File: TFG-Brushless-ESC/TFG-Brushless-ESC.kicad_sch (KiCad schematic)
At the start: 41 parts, among them J1 POWER IN, J2 USB C Receptacle, J3 SWD, J4 MOTOR, SW1 BOOT0, SW2 NRST, SW3 USER, U1 LM317, U2 STM32F411CEUx, Y1 25MHz, Y2 32.768kHz

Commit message: Renaming
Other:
- company: (none) -> Adrián Teixeira de Uña
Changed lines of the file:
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@@
 	(title_block
 		(title "RTSpeed")
+		(date "2024-04-17")
+		(rev "alpha-1.0")
+		(company "Adrián Teixeira de Uña")
 	)
 	(junction

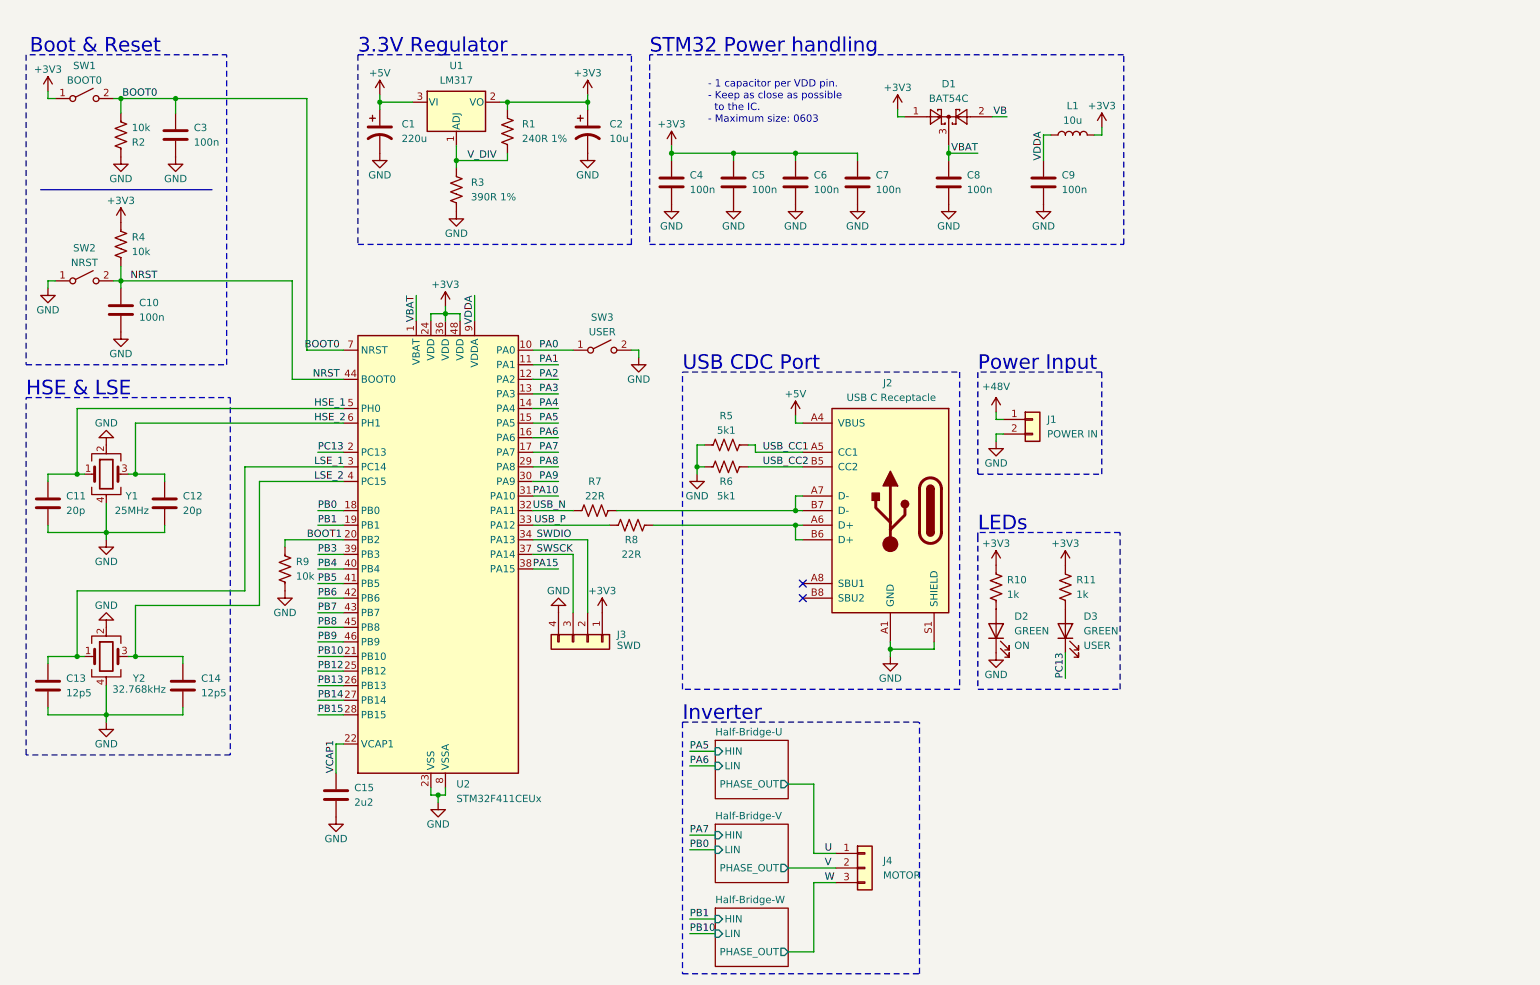
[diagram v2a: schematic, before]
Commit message: Attempt at implementing regenerative braking
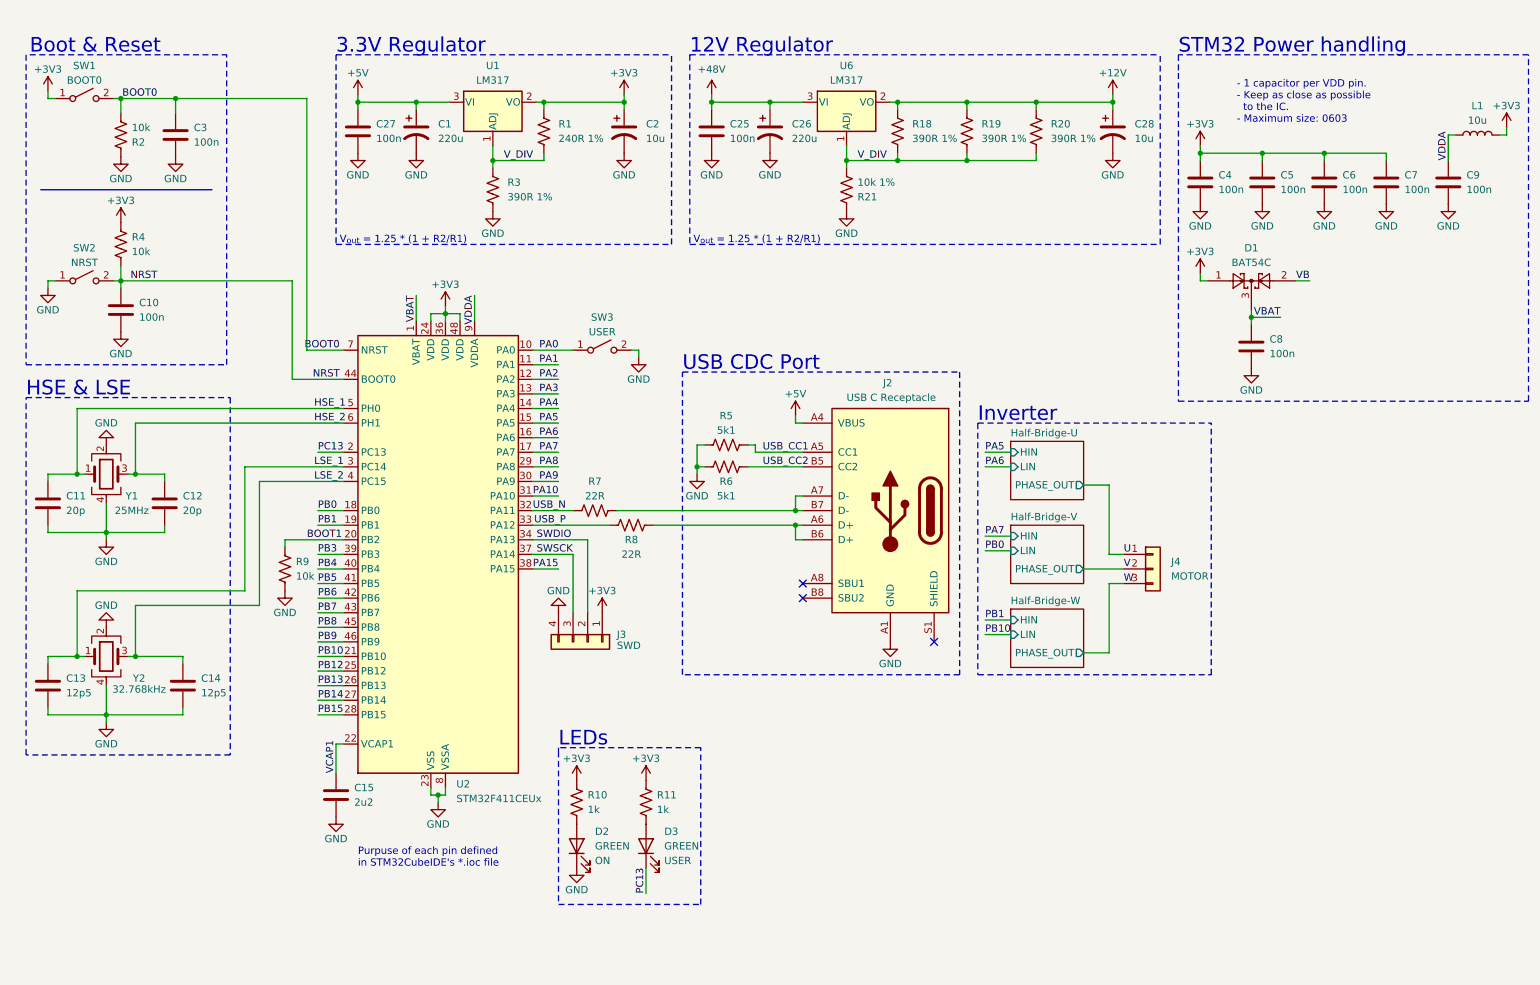
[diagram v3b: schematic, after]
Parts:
- removed J1: POWER IN, symbol Connector_Generic:Conn_01x02
- added C25, C27: 100n, Capacitor_SMD:C_0603_1608Metric, symbol Device:C
- added C26: 220u, Capacitor_THT:CP_Radial_D5.0mm_P2.00mm, symbol Device:C_Polarized_US
- added C28: 10u, Capacitor_THT:CP_Radial_D5.0mm_P2.00mm, symbol Device:C_Polarized_US
- added R18, R19, R20: 390R 1%, Resistor_SMD:R_0603_1608Metric, symbol Device:R_US
- added R21: 10k 1%, Resistor_SMD:R_0603_1608Metric, symbol Device:R_US
- added U6: LM317, Package_TO_SOT_THT:TO-220-3_Vertical, symbol Regulator_Linear:LM317_TO-220
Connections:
- net +48V: now also C25.1, C26.1, U6.3 (VI)
- net +5V: now also C27.1
- net GND: now also C25.2, C26.2, C27.2, C28.2, R21.1; no longer J2.S1 (SHIELD)
- net V_DIV: now also R18.2, R19.2, R20.2, R21.2, U6.1 (ADJ)
- new net +12V: C28.1, R18.1, R19.1, R20.1, U6.2 (VO)
- no-connect marks 2 -> 3
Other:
- note added: "12V Regulator"
- note added: "Purpuse of each pin defined in STM32CubeIDE's *.ioc file"
- note added: "V_{out} = 1.25 * (1 + R2/R1)"
- note removed: "Power Input"
- moved on the sheet: C1, C2, C4, C5, C6, C7, C8, C9, D1, D2, D3, J4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

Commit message: Added current and voltage sensing
Other changes: removed BAT Diode since it will not be used, renamed pins of STM32
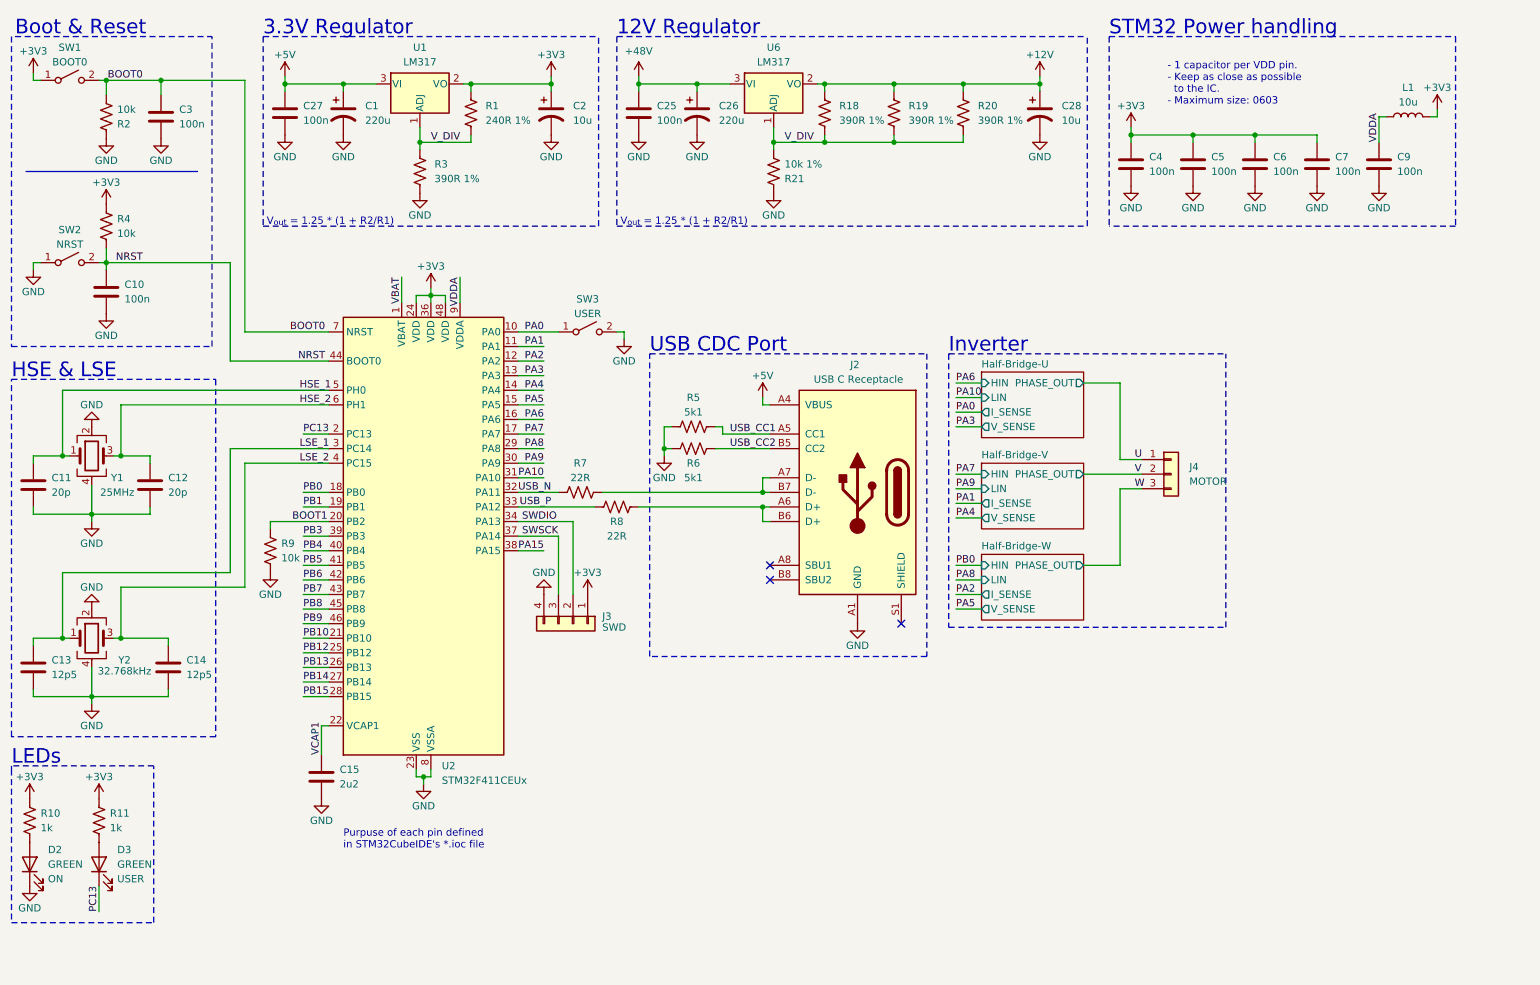
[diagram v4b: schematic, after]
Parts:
- removed C8: 100n, Capacitor_SMD:C_0603_1608Metric, symbol Device:C
- removed D1: BAT54C, Package_TO_SOT_SMD:SOT-23, symbol Diode:BAT54C
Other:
- sheet Half-Bridge-U ports: added I_SENSE, V_SENSE; removed none
- sheet Half-Bridge-V ports: added I_SENSE, V_SENSE; removed none
- sheet Half-Bridge-W ports: added I_SENSE, V_SENSE; removed none
- moved on the sheet: C1, C10, C11, C12, C13, C14, C15, C2, C25, C26, C27, C28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

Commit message: Footprint corrections
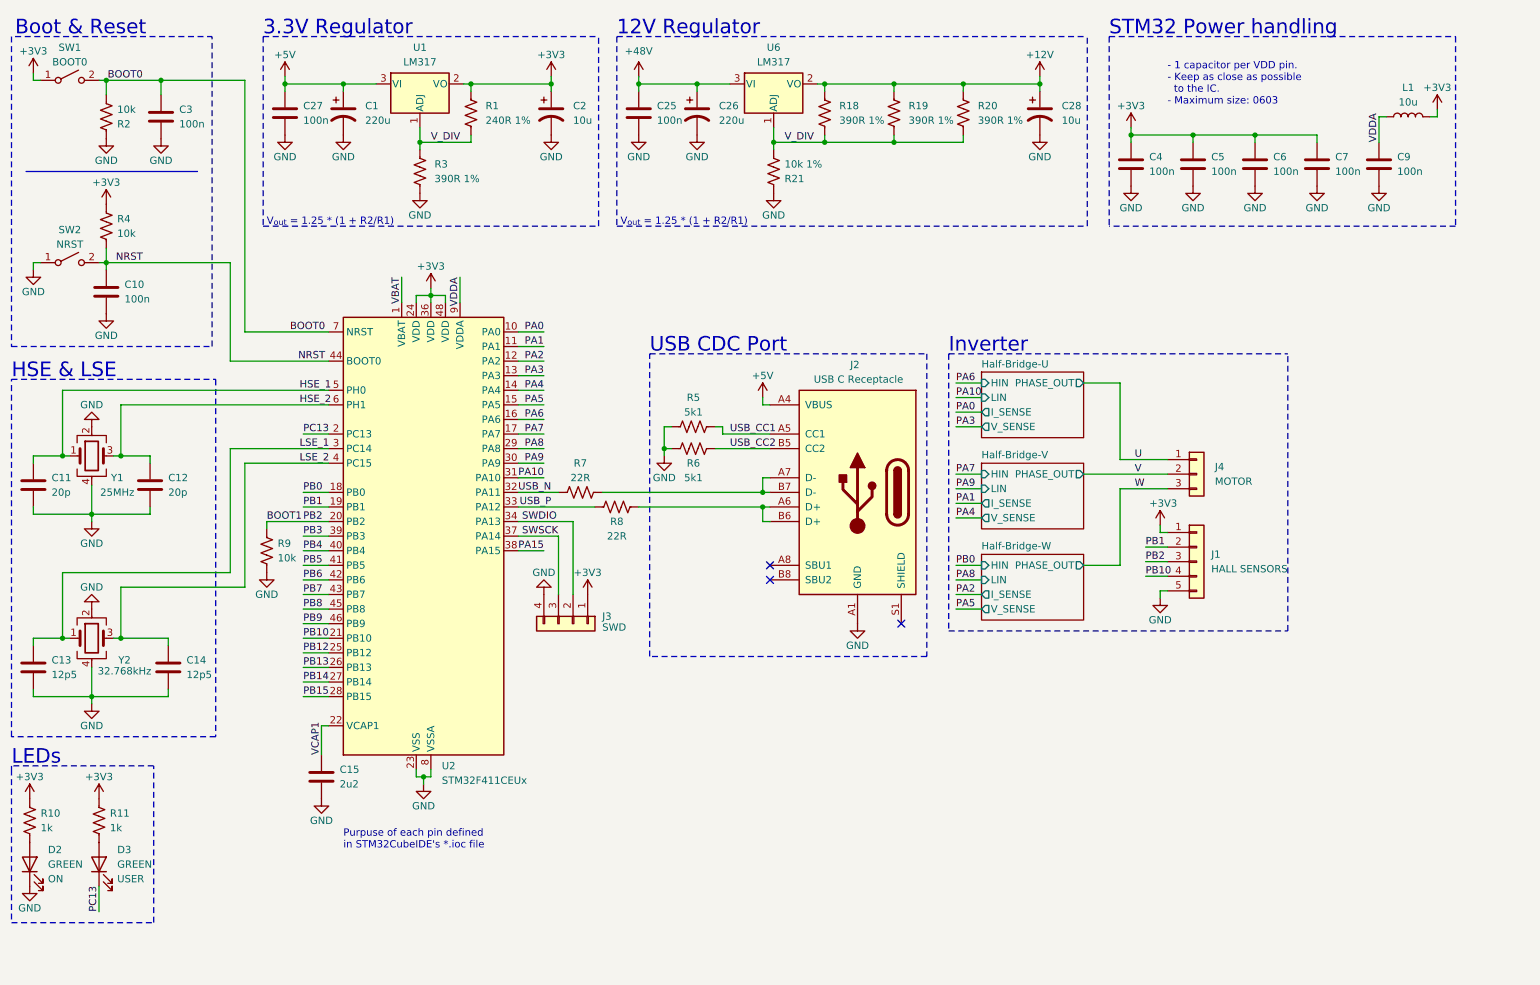
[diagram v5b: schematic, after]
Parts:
- removed SW3: USER, Button_Switch_SMD:SW_Push_1P1T_NO_6x6mm_H9.5mm, symbol Switch:SW_SPST
- added J1: HALL SENSORS, Connector_PinHeader_2.54mm:PinHeader_1x05_P2.54mm_Vertical, symbol Connector_Generic:Conn_01x05
- J4: footprint (none) -> Connector_PinHeader_2.54mm:PinHeader_1x03_P2.54mm_Vertical
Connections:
- net +3V3: now also J1.1 (Pin_1)
- net BOOT1: now also J1.3 (Pin_3)
- net GND: now also J1.5 (Pin_5)
- net PB1: now also J1.2 (Pin_2)
- net PB10: now also J1.4 (Pin_4)
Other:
- moved on the sheet: J4, R9

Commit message: Half bridges done
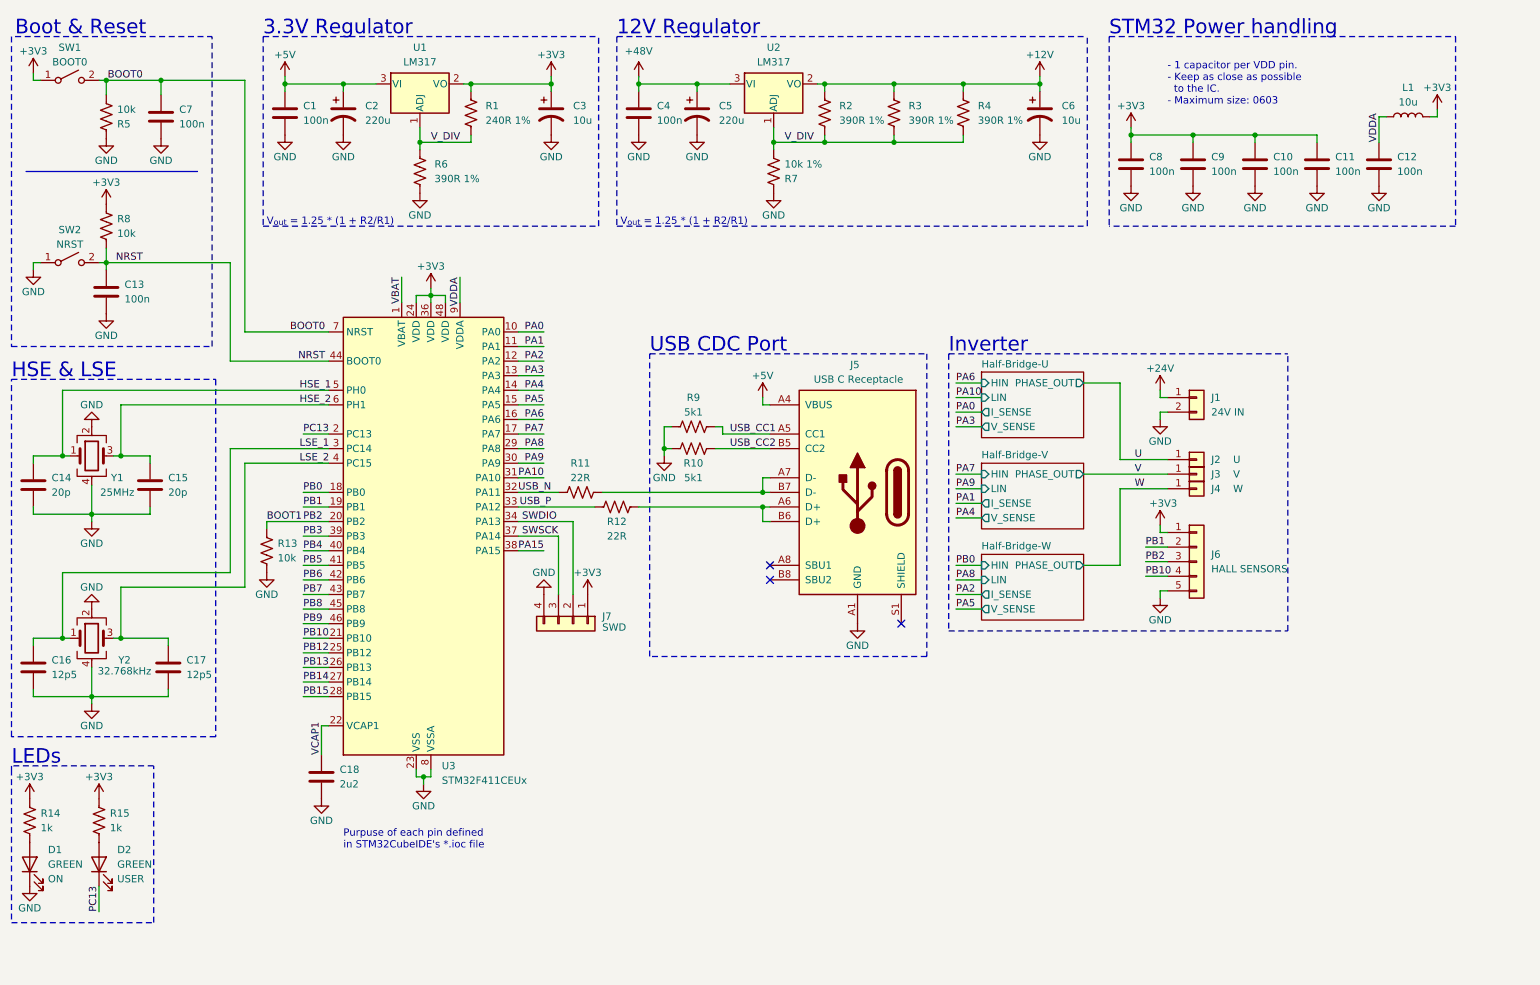
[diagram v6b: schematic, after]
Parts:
- removed J4: MOTOR, Connector_PinHeader_2.54mm:PinHeader_1x03_P2.54mm_Vertical, symbol Connector_Generic:Conn_01x03
- added J1: 24V IN, TFG-Brushless-ESC:Large_Conn_01x02, symbol Connector_Generic:Conn_01x02
- added J2: U, TFG-Brushless-ESC:Large_Conn_01x01, symbol Connector_Generic:Conn_01x01
- added J3: V, TFG-Brushless-ESC:Large_Conn_01x01, symbol Connector_Generic:Conn_01x01
- added J4: W, TFG-Brushless-ESC:Large_Conn_01x01, symbol Connector_Generic:Conn_01x01
- renumbered C27 to C1, C6 to C10, C7 to C11, C9 to C12, C10 to C13, C11 to C14, C12 to C15, C13 to C16, C14 to C17, C15 to C18, C1 to C2, C2 to C3, C25 to C4, C26 to C5, C28 to C6, C3 to C7, C4 to C8, C5 to C9, D2 to D1, D3 to D2, J2 to J5, J1 to J6, J3 to J7, R6 to R10, R7 to R11, R8 to R12, R9 to R13, R10 to R14, R11 to R15, R18 to R2, R19 to R3, R20 to R4, R2 to R5, R3 to R6, R21 to R7, R4 to R8, R5 to R9, U6 to U2, U2 to U3
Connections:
- net GND: now also J1.2 (Pin_2)
- net U: now also J2.1 (Pin_1)
- net V: now also J3.1 (Pin_1)
- net W: now also J4.1 (Pin_1)
- new net +24V: J1.1 (Pin_1)
